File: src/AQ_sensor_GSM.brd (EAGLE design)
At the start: 110 x 64 mm, 120 parts, among them IC1 MIC29302WU, J1 F-1X03-SIP-100-32, J3 PJ-002BH, Q1 MMBT2222, Q2 MMBT2222, Q3 MMBT2222, Q4 MMBT2222, Q5 MMBT2222, Q6 MMBT2222, Q7 MMBT2222, U3 TEXAS_INSTRUMENTS_LM1117IMP-3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, U5 TXS0108EPWR, X1 53048-08

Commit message: Routed
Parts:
- removed C22, C25, C26, C27, C5: ECA-1HM220, Resistor_Capacitor:CAP_RADIAL_2MM
- removed C6: EEEFN1C471P, EEEFN1C471P:CAP_EEEFN1C471P
- removed C7: 100nf, 06035C104K4T2A:CAPC1608X90N
- removed CHARGE: PCM12SMTR, AQ_sensor_MRC:SW_PCM12SMTR
- removed C_P: ORANGE, led:CHIP-LED0603
- removed D5: ESD56151W04, 4.7V TVS Diode:DIO_1N4148WS_RR
- removed IC1: MIC29302WU, MIC29302WU:TO263-5
- removed LIPO/BUCK, USB/BATT: TL2285EE, TL2285EE:SW_TL2285EE
- removed POWER: RED, led:CHIP-LED0603
- removed Q1: MMBT2222, MMBT2222_:SOT23-BEC
- removed R10: 47K, rcl:R0603
- removed R11: 470R, rcl:R0603
- removed R9: 100k, rcl:R0603
- removed SOLAR_IN: 10118192-0001LF, AQ_sensor_GSM:AMPHENOL_10118192-0001LF
- removed U$1: (no value), MT2492:SOT95P280X145-6N
- removed X1: 53048-08, AQ_sensor_GSM:53048-08
- added 5V: 2828XX-2282834-2, Connector:TERMBLK_254-2N
- added BATT, PWR: TL2285EE, TL2285EE:SW_TL2285EE
- added CHARGER: KMR621NGLFS, AQ_sensor_GSM:SW_KMR621NGLFS
- added CHARGING, PWR_ON: ORANGE, led:CHIP-LED0603
- added D4, D6, D7: SS54-HF, SS54-HF schottkey Diode:DIOM5025X220N
- added GPIO, PROG: PINHD-1X4, Connector:1X04
- added J2: 53261-0871, 53261-0871:MOLEX_53261-0871
- added MT2492: MT2492, MT2492:SOT95P280X145-6N
- added PO: RED, led:CHIP-LED0603
- C2: value 470uf -> 100uF; device T495X477K010ATE100:CAPMP7343X430N -> rcl:PANASONIC_D
- C3: value 100nf -> 100uF; device 06035C104K4T2A:CAPC1608X90N -> rcl:PANASONIC_D
- R2: value 51K -> 1k; device rcl:R0603 -> SparkFun-Resistors:0603
- R3: value 4.7K -> 47k; device rcl:R0603 -> SparkFun-Resistors:0603
- R8: value 47K -> 10k; device rcl:R0603 -> SparkFun-Resistors:0603
- moved H3 116.7 mm to (106.3, 3.68), turned to 180 degrees
- moved H4 116.4 mm to (106.3, 59.7), turned to 180 degrees
- moved H2 116.3 mm to (4.26, 3.68), turned to 180 degrees
- moved H1 116.0 mm to (4.26, 59.7), turned to 180 degrees
- moved GPS 107.5 mm to (106.3, 16.7), turned to 180 degrees
- moved PMS 106.9 mm to (100.7, 60.8), turned to 0 degrees
- moved GSM_ANT 105.3 mm to (107.5, 27.4), turned to 180 degrees
- moved GSM 104.9 mm to (107.7, 35.3), turned to 0 degrees
- moved ESP_RESET 104.5 mm to (5.21, 42.0), turned to 180 degrees
- moved 100% 103.0 mm to (3.02, 35.9), turned to 270 degrees
- moved 50% 103.0 mm to (3.02, 29.0), turned to 270 degrees
- moved 75% 103.0 mm to (3.02, 32.4), turned to 90 degrees
- moved 25% 102.9 mm to (3.10, 25.7), turned to 90 degrees
- moved BT_ANT 101.9 mm to (95.2, 1.96), turned to 180 degrees
- moved R22 98.2 mm to (100.2, 49.7), flipped to the bottom
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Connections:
- net USB_VBUS renamed G_USB_VBUS
- removed net +5V: R14.2, SV2.1, U3.3, USB/BATT.3, USB/BATT.4, X1.8
- removed net 3.8V: C6.1, C7.2, D5.C, IC1.4, LIPO/BUCK.1, LIPO/BUCK.6, R11.2, R9.2
- removed net 4.2V: C29.1, L2.2, LIPO/BUCK.2, LIPO/BUCK.5, R19.2, U$2.6
- removed net BVIN: C5.1, J3.1, R7.2, SOLAR_IN.1, U$1.5
- removed net D+: PB_IN.3, SOLAR_IN.3
- removed net D-: PB_IN.2, SOLAR_IN.2
- removed net N$36: Q1.B, R3.2
- removed net N$37: Q1.E, R8.2
- removed net N$38: IC1.5, R10.2, R9.1
- removed net TF-CLK: SV2.7
- removed net TF-CS: SV2.9
- removed net TF-MISO: SV2.8
- removed net TF-MOSI: SV2.10
- new net 4.5-16V: C3.+, MT2492.5, PWR.3, PWR.4, R2.1, R7.2
- new net 5VT: D4.1, PWR.2, PWR.5
- new net BMSV: R3.2, R8.1, SV2.15
- new net G_ADC0: EC200_GSM.45, GPIO.1
- new net G_ADC1: EC200_GSM.44, GPIO.2
- new net G_ADC2: EC200_GSM.43
- new net G_GPIO1: EC200_GSM.126
- new net G_I2C_SCL: EC200_GSM.41, GPIO.4
- new net G_I2C_SDA: EC200_GSM.42, GPIO.3
- new net G_SPI_CLK: EC200_GSM.40
- new net G_SPI_CS: EC200_GSM.37
- new net G_SPI_MISO: EC200_GSM.39
- new net G_SPI_MOSI: EC200_GSM.38
- new net G_USB_BOOT: EC200_GSM.115, PROG.1
- new net G_USB_D+: EC200_GSM.69, PB_IN.3
- new net G_USB_D-: EC200_GSM.70, PB_IN.2
- new net LBV: BATT.3, BATT.4, LIPO.1, R3.1
- new net N$59: D4.2, PB_IN.1
- new net N$60: D7.1, J3.2, J3.3
- new net N$61: D6.2, J3.1
- net 5V_IN: now also 5V.1; no longer C22.1
- net 5V_OUT: now also C2.+, J2.8, R14.2, SV2.1, U3.3; no longer C25.1, C26.1, C27.1, USB/BATT.2, USB/BATT.5
- net GND: now also 5V.2, C2.-, C3.-, CHARGER.2_1, CHARGER.2_2, CHARGING.C, D7.2, J2.7, MT2492.2, PO.C, PROG.4, PWR_ON.C, R8.2; no longer C2.2, C22.2, C25.2, C26.2, C27.2, C3.1, C5.2, C6.2, C7.1, CHARGE.2, C_P.C, D5.A, IC1.3, J3.2, J3.3, POWER.C, R10.1, R11.1, R8.1, SOLAR_IN.4, SOLAR_IN.5, SOLAR_IN.SH1, SOLAR_IN.SH2, SOLAR_IN.SH3, SOLAR_IN.SH4, SOLAR_IN.SH5, SOLAR_IN.SH6, U$1.2, X1.7
- net MCU_RXD: now also PROG.2
- net MCU_TXD: now also PROG.3
- net N$10: now also MT2492.3; no longer U$1.3
- net N$11: now also MT2492.4; no longer U$1.4
- net N$20: now also CHARGER.1_1, CHARGER.1_2; no longer CHARGE.1
- net N$25: now also PO.A; no longer POWER.A
- net N$3: now also MT2492.1; no longer U$1.1
- net N$35: now also PWR_ON.A, R2.2; no longer IC1.1, Q1.C, R2.1
- net N$46: now also CHARGING.A; no longer C_P.A
- net N$6: now also MT2492.6; no longer U$1.6
- net PMS_RX: now also J2.5; no longer X1.5
- net PMS_TX: now also J2.4; no longer X1.4
- net VBAT_EN: no longer R3.1
- net VUSB: now also D6.1, PWR.1, PWR.6; no longer C2.1, C3.2, IC1.2, PB_IN.1, R2.2, USB/BATT.1, USB/BATT.6
- net V_LIPO: now also BATT.2, BATT.5, C29.1, L2.2, R19.2, U$2.6; no longer LIPO.1, LIPO/BUCK.3, LIPO/BUCK.4
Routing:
- net V_LIPO: track 0.00 -> 258.7 mm, vias 0 -> 16
- net 5V_IN: track 0.00 -> 214.6 mm, vias 0 -> 16
- net G_ADC0: track 0.00 -> 174.7 mm, vias 0 -> 10
- net MCU_RXD: track 0.00 -> 167.8 mm, vias 0 -> 7
- net SIMCLK: track 0.00 -> 167.2 mm, vias 0 -> 11
- net SIMRST: track 0.00 -> 165.3 mm, vias 0 -> 10
- net G_ADC1: track 0.00 -> 161.7 mm, vias 0 -> 3
- net +3V3: track 0.00 -> 159.7 mm, vias 0 -> 10
- net G_I2C_SDA: track 0.00 -> 152.9 mm, vias 0 -> 6
- net G_I2C_SCL: track 0.00 -> 152.2 mm, vias 0 -> 7
- net N$20: track 0.00 -> 134.4 mm, vias 0 -> 2
- net PWRSTAT: track 0.00 -> 133.9 mm, vias 0 -> 3
- net N$14: track 0.00 -> 129.3 mm, vias 0 -> 3
- net 5V_OUT: track 0.00 -> 128.7 mm, vias 0 -> 7
- net GSM_RST: track 0.00 -> 128.3 mm, vias 0 -> 5
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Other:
- board text added: "+"
- board text added: "-"
- board text added: "BATTERY LEVEL"
- board text removed: "PMS5003"

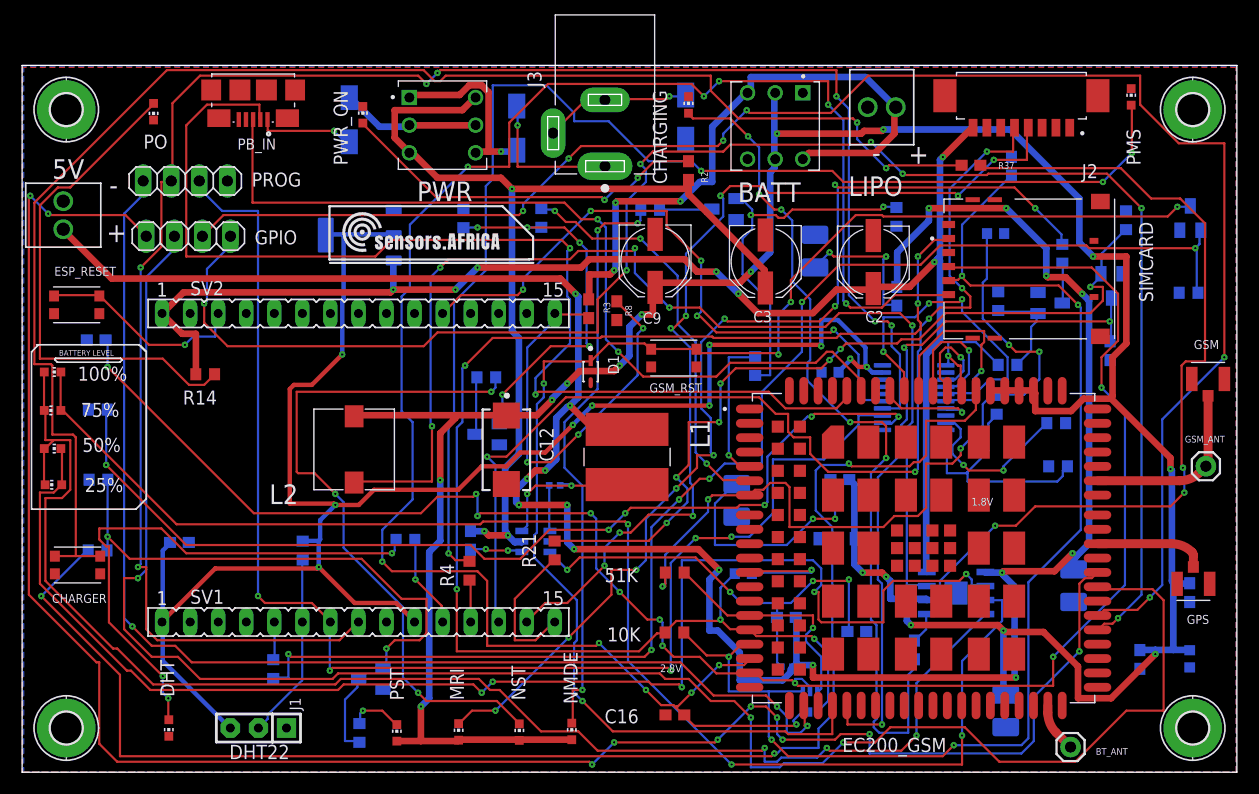
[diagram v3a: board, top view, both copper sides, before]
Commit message: Trace Width updated
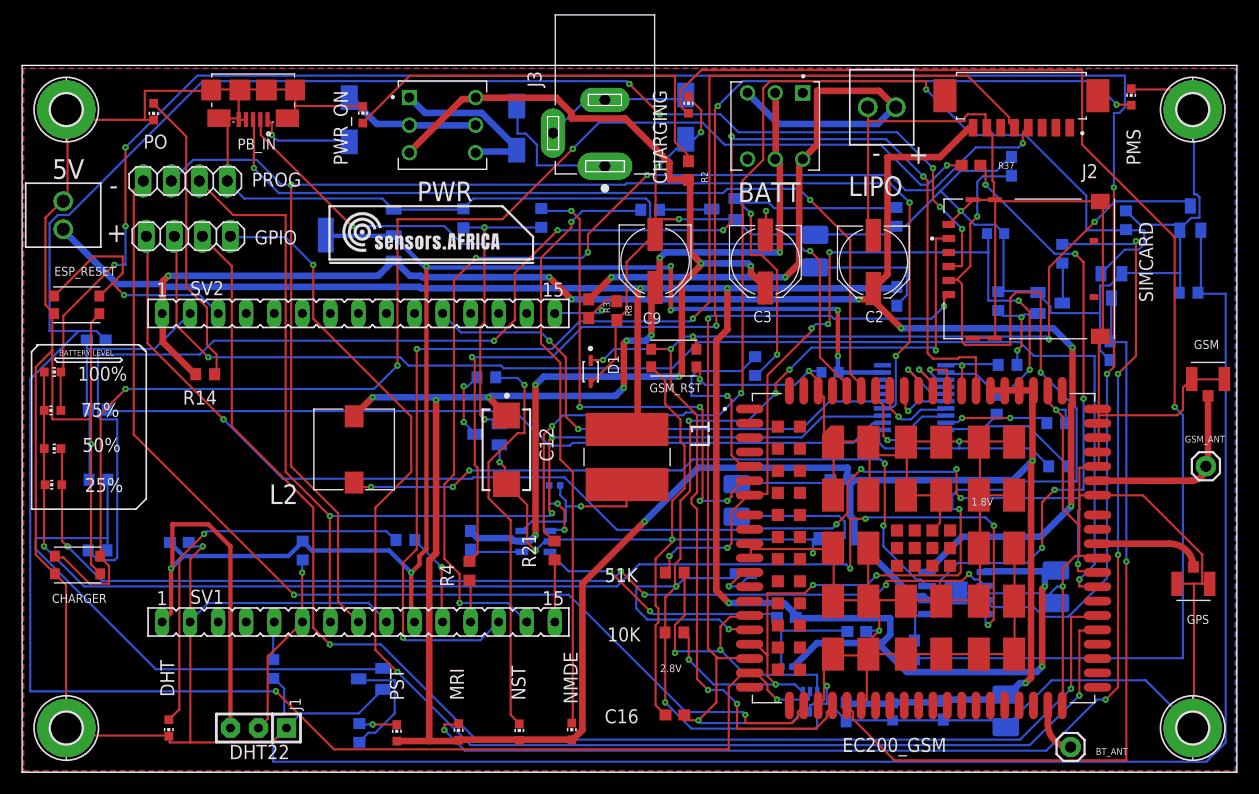
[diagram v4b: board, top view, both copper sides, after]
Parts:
- moved C11 32.9 mm to (74.9, 5.14)
- moved C13 27.3 mm to (79.1, 5.14)
- moved C10 18.4 mm to (83.7, 5.29)
- moved C30 1.60 mm to (93.9, 16.5)
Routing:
- net GND: track 0.00 -> 906.5 mm, vias 0 -> 18
- net SIMCLK: track 167.2 -> 75.4 mm, vias 11 -> 3
- net SIMRST: track 165.3 -> 230.2 mm, vias 10 -> 7
- net G_ADC0: track 174.7 -> 116.3 mm, vias 10 -> 6
- net N$18: track 123.7 -> 179.6 mm, vias 3 -> 5
- net G_ADC1: track 161.7 -> 117.5 mm, vias 3 -> 2
- net N$46: track 78.4 -> 120.9 mm, vias 5 -> 1
- net N$21: track 101.2 -> 62.6 mm
- net MCU_RXD: track 167.8 -> 131.6 mm, vias 7 -> 3
- net 5V_IN: track 214.6 -> 179.5 mm, vias 16 -> 5
- net N$2: track 74.5 -> 107.2 mm, vias 7 -> 3
- net G_USB_D-: track 101.0 -> 69.6 mm
- net BMSV: track 39.0 -> 8.18 mm, vias 3 -> 1
- net N$17: track 126.2 -> 96.2 mm
- net G_I2C_SDA: track 152.9 -> 123.3 mm, vias 6 -> 2
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
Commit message: Routed - Minus DW01
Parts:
- moved L1 35.4 mm to (19.6, 27.9)
- moved C16 6.09 mm to (64.5, 1.63), turned to 0 degrees
- moved L2 3.76 mm to (33.9, 27.8)
- moved 51K 3.69 mm to (61.7, 20.6), turned to 90 degrees
- moved 10K 2.75 mm to (62.0, 11.8), turned to 90 degrees
- moved NST 2.00 mm to (43.3, 3.21)
- moved R4 1.60 mm to (40.8, 19.5)
- moved NMDE 1.51 mm to (48.5, 3.17)
- moved GSM_RST 1.30 mm to (60.4, 37.9)
- moved MRI 1.00 mm to (38.8, 3.23)
- moved C12 1.00 mm to (44.1, 27.9)
- moved R21 0.40 mm to (48.5, 19.4)
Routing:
- net PMS_TX: track 97.4 -> 174.9 mm, vias 5 -> 3
- net SIMRST: track 230.2 -> 156.6 mm
- net N$4: track 101.6 -> 161.7 mm
- net GND: track 906.5 -> 849.0 mm, vias 18 -> 25
- net MAIN_DTR: track 5.77 -> 60.6 mm, vias 1 -> 5
- net N$45: track 60.8 -> 115.2 mm, vias 5 -> 1
- net PMS_RX: track 114.7 -> 167.7 mm, vias 3 -> 4
- net G_ADC1: track 117.5 -> 164.4 mm, vias 2 -> 1
- net N$17: track 96.2 -> 140.0 mm
- net V_LIPO: track 238.4 -> 205.5 mm, vias 11 -> 8
- net N$40: track 9.52 -> 41.7 mm, vias 2 -> 0
- net N$31: track 14.2 -> 45.5 mm, vias 0 -> 4
- net G_USB_D+: track 75.6 -> 106.8 mm, vias 2 -> 6
- net PWRSTAT: track 138.4 -> 107.8 mm
- net N$18: track 179.6 -> 150.0 mm, vias 5 -> 3
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
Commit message: JLCPCB V2
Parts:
- removed U$2: (no value), IP5306:SOIC127P600X165-9T209N
- added C4: 100nf, 06035C104K4T2A:CAPC1608X90N
- added DW01: DW01-P, DW01-P:SOT23-6L
- added IP5306: IP5306, IP5306:SOIC127P600X165-9T209N
- added Q8: FS8205, FS8205:SOT95P280X145-6N
- added R10: 100R, SparkFun-Resistors:0603
- added R9: 1k, SparkFun-Resistors:0603
- R16, R4: value 470 -> 470R
- R6: value 15 -> 15k
- moved Q3 100.6 mm to (3.79, 11.0), flipped to the top, turned to 90 degrees
- moved R22 100.0 mm to (9.08, 8.44), flipped to the top, turned to 90 degrees
- moved Q2 98.0 mm to (17.0, 8.75), flipped to the top
- moved R18 84.6 mm to (28.6, 8.69), flipped to the top, turned to 90 degrees
- moved R37 82.7 mm to (10.3, 21.8)
- moved R20 66.0 mm to (15.5, 17.5), turned to 0 degrees
- moved R29 65.0 mm to (70.4, 17.6)
- moved C17 62.6 mm to (61.8, 8.58), flipped to the top, turned to 180 degrees
- moved C16 57.5 mm to (103.9, 43.6), flipped to the bottom, turned to 90 degrees
- moved C30 56.4 mm to (38.3, 25.9)
- moved C23 51.8 mm to (24.7, 26.0)
- moved R17 51.4 mm to (31.6, 24.2), turned to 180 degrees
- moved C1 51.4 mm to (60.9, 3.12), flipped to the top, turned to 0 degrees
- moved R19 42.2 mm to (32.8, 18.3), turned to 90 degrees
- moved C24 40.7 mm to (24.6, 18.9), turned to 90 degrees
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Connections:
- new net BATT-: C4.2, DW01.6, LIPO.2, Q8.1
- new net N$19: DW01.3, Q8.4
- new net N$37: C4.1, DW01.5, R10.1
- new net N$47: DW01.2, R9.1
- new net N$9: DW01.1, Q8.6
- net 5V_IN: now also IP5306.1; no longer U$2.1
- net 5V_OUT: now also IP5306.8; no longer U$2.8
- net GND: now also IP5306.9, Q8.3, R9.2; no longer LIPO.2, U$2.9
- net LBV: now also R10.2
- net N$14: now also IP5306.4; no longer U$2.4
- net N$17: now also IP5306.2; no longer U$2.2
- net N$18: now also IP5306.3; no longer U$2.3
- net N$21: now also IP5306.7; no longer U$2.7
- net N$45: now also IP5306.5; no longer U$2.5
- net V_LIPO: now also IP5306.6; no longer U$2.6
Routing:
- net +3V3: track 131.1 -> 286.9 mm, vias 7 -> 11
- net N$18: track 150.0 -> 34.7 mm
- net BATT-: track 0.00 -> 113.7 mm
- net N$17: track 140.0 -> 27.2 mm, vias 5 -> 3
- net N$1: track 119.9 -> 13.7 mm
- net N$45: track 115.2 -> 12.6 mm
- net N$20: track 109.5 -> 7.36 mm, vias 6 -> 0
- net N$14: track 149.1 -> 49.9 mm
- net GND: track 849.0 -> 947.9 mm, vias 25 -> 19
- net PMS_TX: track 174.9 -> 88.5 mm, vias 3 -> 0
- net PMS_RX: track 167.7 -> 87.2 mm, vias 4 -> 0
- net 5V_IN: track 184.6 -> 105.8 mm, vias 9 -> 5
- net MCU_DTR: track 45.0 -> 122.2 mm, vias 2 -> 8
- net SIMRST: track 156.6 -> 87.9 mm, vias 7 -> 3
- net V_LIPO: track 205.5 -> 272.0 mm, vias 8 -> 11
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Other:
- board size 110 x 64 mm -> 110.2 x 66.3 mm

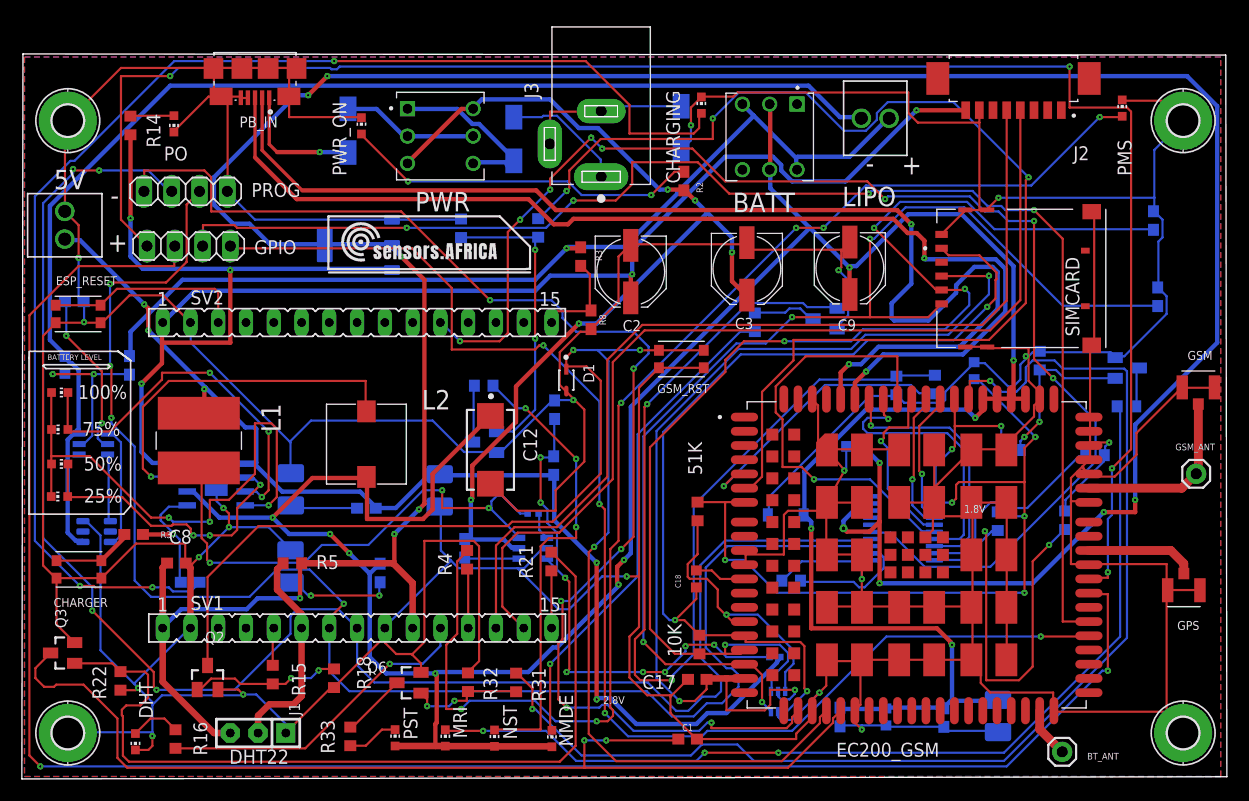
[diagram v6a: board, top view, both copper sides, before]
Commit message: Replaced 5v regulator to lm7805
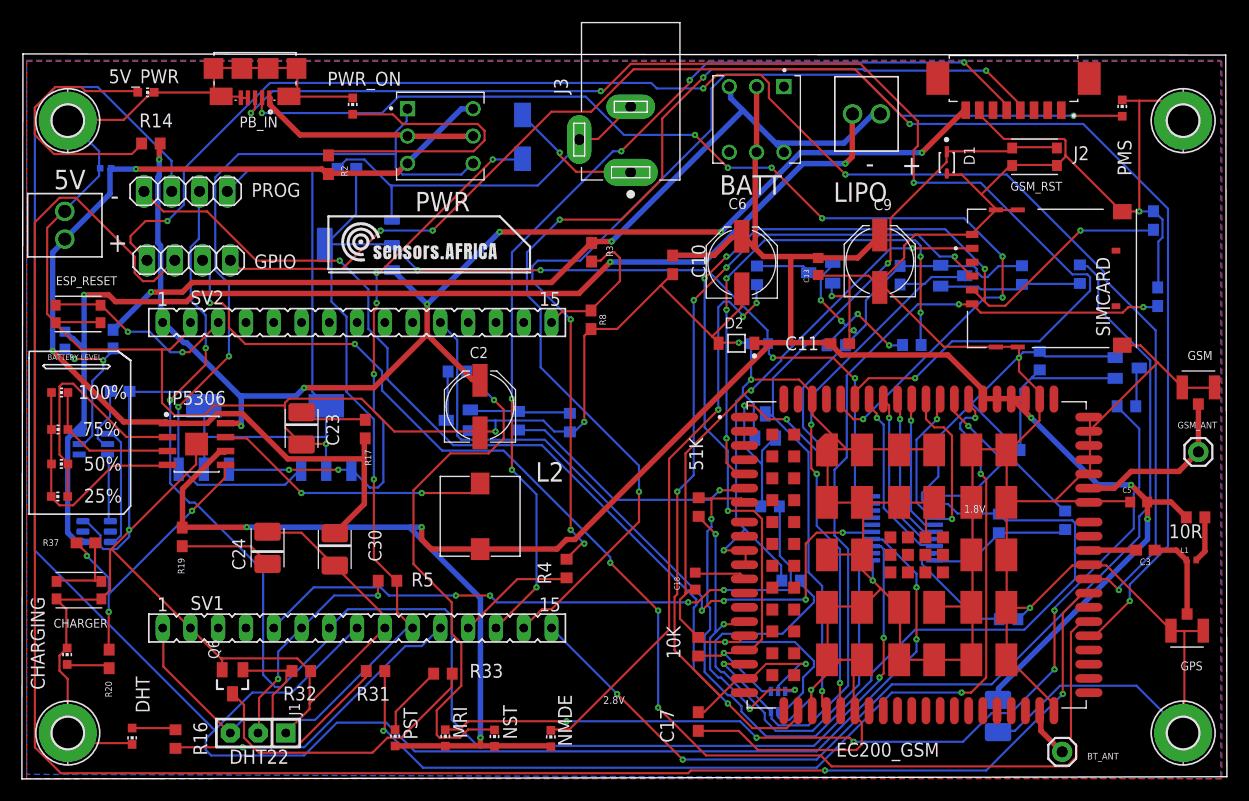
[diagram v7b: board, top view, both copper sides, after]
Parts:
- removed C12: 470uf, T495X477K010ATE100:CAPMP7343X430N
- removed C14: 22nF, SparkFun-Capacitors:0402-TIGHT
- removed D4, D7: SS54-HF, SS54-HF schottkey Diode:DIOM5025X220N
- removed MT2492: MT2492, MT2492:SOT95P280X145-6N
- removed PO: RED, led:CHIP-LED0603
- removed R1: 110k, SparkFun-Resistors:0603
- removed R6: 15k, SparkFun-Resistors:0603
- removed R7: 10k, SparkFun-Resistors:0603
- added 10R: 10R, rcl:R0603
- added 5V_PWR: RED, led:CHIP-LED0603
- added C5: 100nf, 06035C104K4T2A:CAPC1608X90N
- added C6: 100uF, rcl:PANASONIC_D
- added VR1, VR2: LM7805MPX/NOPB, LM7805MPX_NOPB:VREG_LM7805MPX/NOPB
- C3: value 100uF -> 100pF; device rcl:PANASONIC_D -> SparkFun-Capacitors:0603
- L1: value 784787047 -> LQW15AN47NG00D; device Fixed Inductors:784787047 -> LQW15AN47NG00D 47uh:INDC1005X60N
- moved L1 91.4 mm to (107.0, 19.5), turned to 0 degrees
- moved R22 90.4 mm to (91.5, 45.6), flipped to the bottom, turned to 270 degrees
- moved Q3 88.4 mm to (85.2, 45.5), flipped to the bottom
- moved CHARGING 76.8 mm to (4.20, 10.7)
- moved C21 75.8 mm to (7.72, 55.3)
- moved Q2 55.9 mm to (68.0, 31.8), flipped to the bottom
- moved R21 55.0 mm to (96.8, 45.6), flipped to the bottom, turned to 270 degrees
- moved R18 49.6 mm to (73.7, 29.4), flipped to the bottom, turned to 270 degrees
- moved C10 48.3 mm to (59.6, 46.5), flipped to the top
- moved R15 48.0 mm to (68.5, 24.4), flipped to the bottom, turned to 0 degrees
- moved C1 46.7 mm to (80.4, 45.5), flipped to the bottom, turned to 90 degrees
- moved C3 44.6 mm to (102.8, 20.4), turned to 180 degrees
- moved C13 41.7 mm to (72.9, 46.3), flipped to the top
- moved D1 40.1 mm to (84.7, 55.8)
- moved C8 39.3 mm to (29.8, 55.3), flipped to the bottom
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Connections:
- removed net 4.5-16V: C3.+, MT2492.5, PWR.3, PWR.4, R2.1, R7.2
- removed net N$11: MT2492.4, R7.1
- removed net N$59: D4.2, PB_IN.1
- removed net N$6: C14.2, L1.1, MT2492.6
- removed net N$60: D7.1, J3.2, J3.3
- removed net VUSB: D6.1, PWR.1, PWR.6
- new net N$36: D6.1, VR1.1, VR2.1
- new net N$38: PWR.1, PWR.6, VR1.3, VR2.3
- net 5VT: now also PB_IN.1; no longer D4.1
- net 5V_IN: now also PWR.3, PWR.4, R2.1; no longer L1.2, R1.2
- net GND: now also 5V_PWR.C, C21.2, C5.1, C6.-, J3.2, J3.3, VR1.2, VR1.4, VR2.2, VR2.4; no longer C12.2, C3.-, D7.2, MT2492.2, PO.C, R6.1
- net GNSS_ANT: now also C3.2; no longer GPS.1
- net N$10: now also C3.1, GPS.1, L1.1; no longer C21.2, MT2492.3, R1.1, R6.2
- net N$25: now also 5V_PWR.A; no longer PO.A
- net N$3: now also 10R.1, L1.2; no longer C14.1, MT2492.1
- net V_LIPO: now also 10R.2, C5.2, C6.+; no longer C12.1
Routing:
- net +3V3: track 286.9 -> 147.3 mm, vias 11 -> 5
- net N$46: track 120.6 -> 3.99 mm, vias 3 -> 0
- net PWRKEY_0: track 5.24 -> 95.5 mm, vias 0 -> 2
- net 4.5-16V: track 88.3 -> 0.00 mm, vias 5 -> 0
- net NETSTAT: track 107.4 -> 23.7 mm, vias 3 -> 1
- net GND: track 947.9 -> 870.1 mm, vias 19 -> 14
- net N$26: track 94.0 -> 16.5 mm, vias 2 -> 4
- net N$38: track 0.00 -> 72.5 mm, vias 0 -> 2
- net GSM_RST: track 135.4 -> 70.8 mm, vias 3 -> 2
- net N$2: track 77.2 -> 13.1 mm
- net MCU_DTR: track 122.2 -> 62.2 mm, vias 8 -> 4
- net GSM_RST_O: track 3.49 -> 57.9 mm, vias 0 -> 4
- net N$36: track 0.00 -> 52.4 mm, vias 0 -> 6
- net N$6: track 47.8 -> 0.00 mm, vias 3 -> 0
- net V_LIPO: track 272.0 -> 224.9 mm, vias 11 -> 6
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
